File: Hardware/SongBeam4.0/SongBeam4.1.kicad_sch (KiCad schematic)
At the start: 140 parts, among them J1 Conn_01x02, J10 732511150, J11 Conn_01x02, J12 Conn_01x02, J13 Conn_01x01, J2 RJ45, J3 RJ45, J4 Conn_01x07, J5 Conn_01x04, J6 Conn_01x07, J7 Conn_01x04, J8 Conn_01x06, J9 USB_B_Micro, Q2 DTC143ZEBTL, SW2 PTS815 SJM 250 SMTR LFS, SW3 PTS815 SJM 250 SMTR LFS, U1 IM66D132H, U10 Teensy4.1, U11 BQ25185DLHR, U12 AO6604, U13 TPS62842DGRR, U14 TPL5111DDCR, U15 AO6604, U16 TXS0108EPW, U17 LP5907MFX-1.8/NOPB, U19 L86-M33, U2 IM66D132H, U20 AO3407A, U3 IM66D132H, U4 IM66D132H, U5 IM66D132H, U6 IM66D132H, U7 IM66D132H, U8 IM66D132H, U9 PCMD3180IRTWR

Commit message: added a version for manual routing
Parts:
- added F1: Polyfuse, MINISMDC050F-2:MINISMDC050F2, symbol Device:Polyfuse
- R24: value 300 -> 300R
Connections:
- net PWR is gone; now on net +3.3V: J1.1 (Pin_1), JP1.2 (B), U10.48 (VIN)
- net +5V: now also C41.1, R28.1, TP1.1, U12.2 (S2), U13.5 (EN), U13.6 (VIN); no longer F3.1
- net GND: no longer J3.1, J3.2
- net VBAT: now also F1.2; no longer C27.2, U11.2 (BAT)
- net VBUS: now also F3.2; no longer C29.2, U11.10 (IN)
- new net: C29.2, F3.1, U11.10 (IN)
- new net: C27.2, F1.1, U11.2 (BAT)
- no-connect marks 45 -> 47
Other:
- moved on the sheet: C27, C29, F3

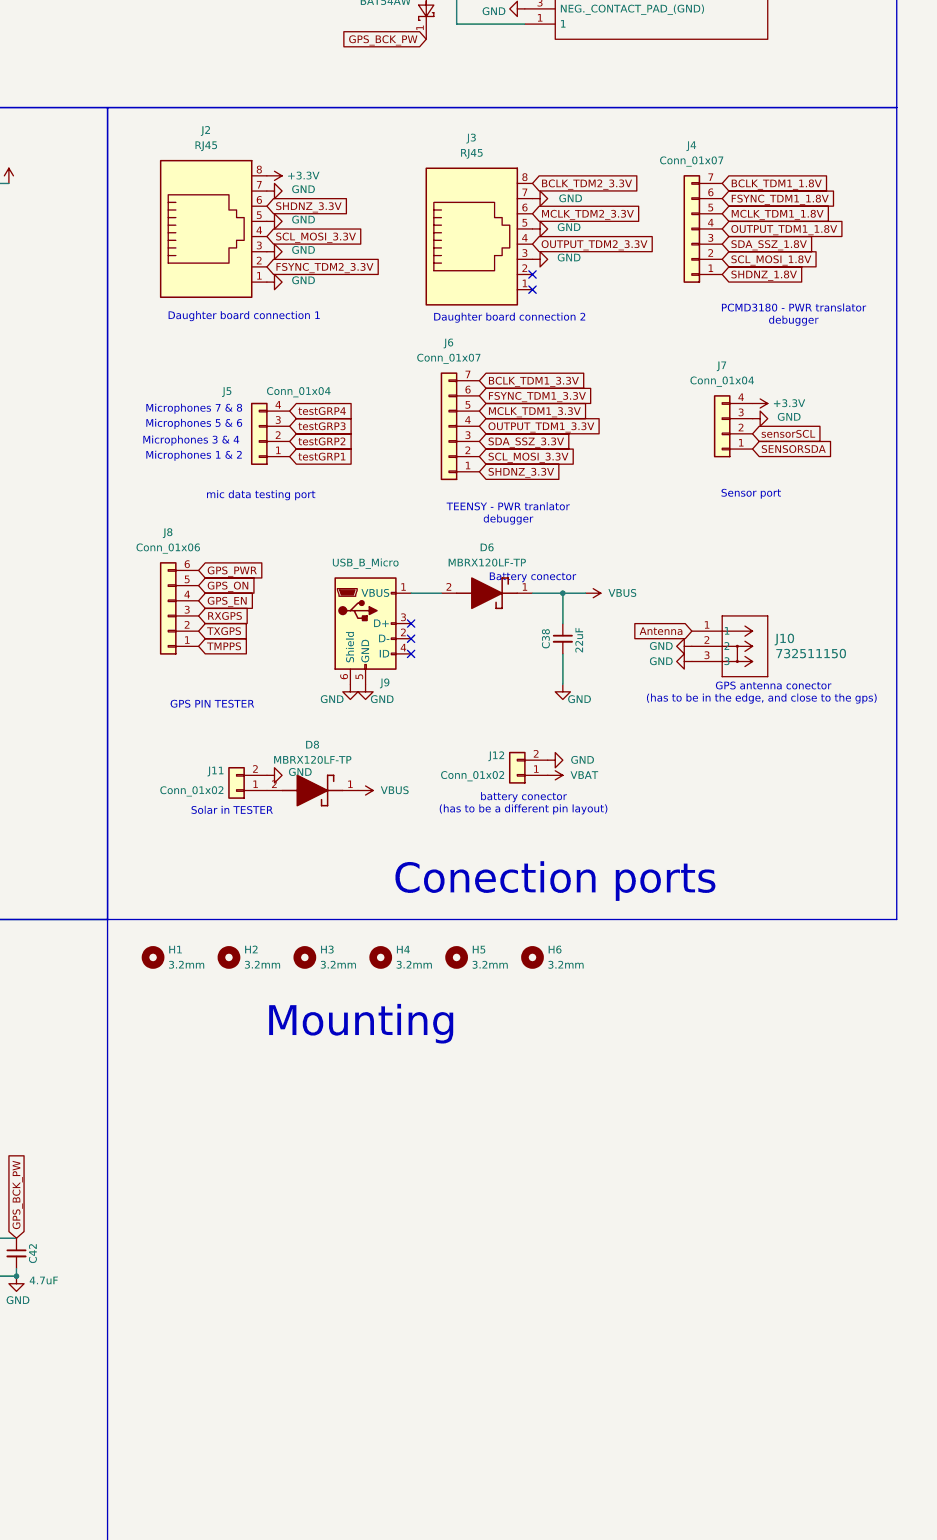
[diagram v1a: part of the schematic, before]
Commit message: ethernet port updated, fixed flaws 1.1 DB
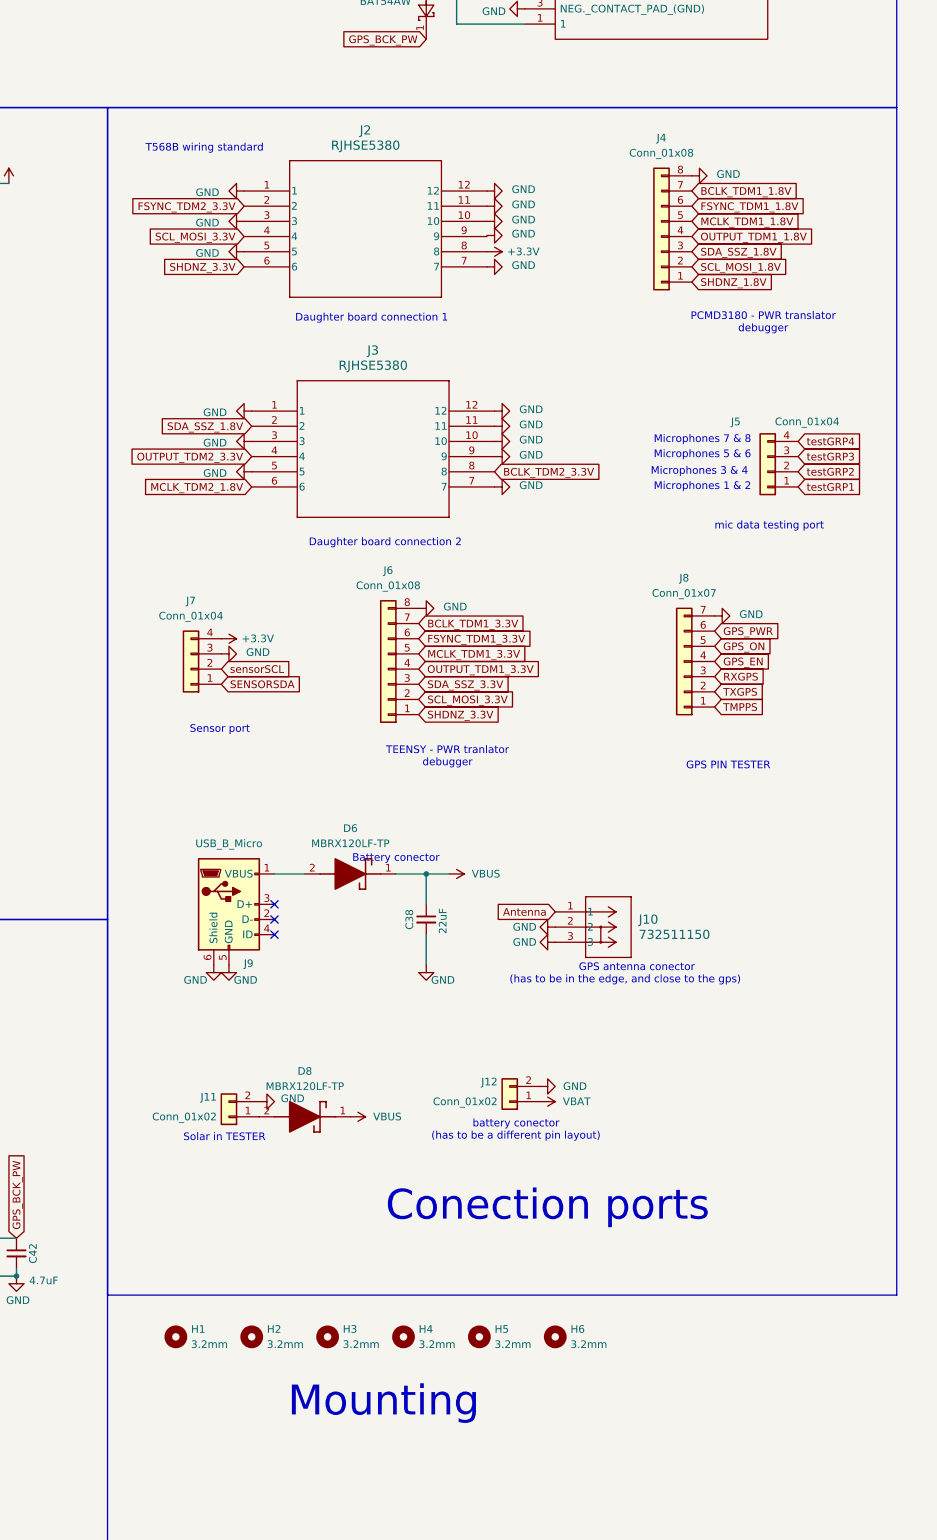
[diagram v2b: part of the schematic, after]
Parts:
- removed J2, J3: RJ45, RJHSE-3380:CONN_RJHSE-3380_AMP, symbol Connector:RJ45
- removed J4, J6: Conn_01x07, Connector_PinHeader_1.00mm:PinHeader_1x07_P1.00mm_Vertical, symbol Connector_Generic:Conn_01x07
- removed J8: Conn_01x06, Connector_PinHeader_1.00mm:PinHeader_1x06_P1.00mm_Vertical, symbol Connector_Generic:Conn_01x06
- added J2, J3: RJHSE5380, RJHSE5380_AMP, symbol Ethernet R/A:RJHSE5380
- added J4, J6: Conn_01x08, symbol Connector_Generic:Conn_01x08
- added J8: Conn_01x07, symbol Connector_Generic:Conn_01x07
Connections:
- net +3.3V: now also J2.8
- net BCLK_TDM1_1.8V: now also J4.7 (Pin_7)
- net BCLK_TDM1_3.3V: now also J6.7 (Pin_7)
- net BCLK_TDM2_3.3V: now also J3.8
- net FSYNC_TDM1_1.8V: now also J4.6 (Pin_6)
- net FSYNC_TDM1_3.3V: now also J6.6 (Pin_6)
- net FSYNC_TDM2_3.3V: now also J2.2
- net GND: now also J2.1, J2.10, J2.11, J2.12, J2.3, J2.5, J2.7, J3.1, J3.10, J3.11, J3.12, J3.3, J3.5, J3.7, J3.9, J4.8 (Pin_8), J6.8 (Pin_8), J8.7 (Pin_7)
- net GPS_EN: now also J8.4 (Pin_4)
- net GPS_ON: now also J8.5 (Pin_5)
- net GPS_PWR: now also J8.6 (Pin_6)
- net MCLK_TDM1_1.8V: now also J4.5 (Pin_5)
- net MCLK_TDM1_3.3V: now also J6.5 (Pin_5)
- net OUTPUT_TDM1_1.8V: now also J4.4 (Pin_4)
- net OUTPUT_TDM1_3.3V: now also J6.4 (Pin_4)
- net OUTPUT_TDM2_3.3V: now also J3.4
- net RXGPS: now also J8.3 (Pin_3)
- net SCL_MOSI_1.8V: now also J4.2 (Pin_2)
- net SCL_MOSI_3.3V: now also J2.4, J6.2 (Pin_2)
- net SDA_SSZ_1.8V: now also J3.2, J4.3 (Pin_3)
- net SDA_SSZ_3.3V: now also J6.3 (Pin_3)
- net SHDNZ_1.8V: now also J4.1 (Pin_1)
- net SHDNZ_3.3V: now also J2.6, J6.1 (Pin_1)
- net TMPPS: now also J8.1 (Pin_1)
- net TXGPS: now also J8.2 (Pin_2)
- new net MCLK_TDM2_1.8V: J3.6
- no-connect marks 47 -> 45
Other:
- note added: "T568B wiring standard"
- moved on the sheet: C38, D6, D8, H1, H2, H3, H4, H5, H6, J10, J11, J12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

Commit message: implemented  ethernet port pcb R/a
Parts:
- J11, J12: footprint Connector_PinHeader_1.00mm:PinHeader_1x02_P1.00mm_Vertical -> Connector_PinHeader_2.00mm:PinHeader_1x02_P2.00mm_Vertical_SMD_Pin1Right
- J13: footprint Connector_PinHeader_1.00mm:PinHeader_1x01_P1.00mm_Vertical -> Connector_PinHeader_2.00mm:PinHeader_1x01_P2.00mm_Vertical
- J2, J3: footprint RJHSE5380_AMP -> RJHSE5380:RJHSE5380_AMP
- J4, J6: footprint (none) -> Connector_PinHeader_2.00mm:PinHeader_1x08_P2.00mm_Vertical
- J8: footprint (none) -> Connector_PinHeader_2.00mm:PinHeader_1x07_P2.00mm_Vertical
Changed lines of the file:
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@@
 			)
 		)
-		(property "Footprint" ""
+		(property "Footprint" "Connector_PinHeader_2.00mm:PinHeader_1x08_P2.00mm_Vertical"
 			(at 496.57 247.65 0)
 			(effects
@@
 			)
 		)
-		(property "Footprint" "Connector_PinHeader_1.00mm:PinHeader_1x01_P1.00mm_Vertical"
+		(property "Footprint" "Connector_PinHeader_2.00mm:PinHeader_1x01_P2.00mm_Vertical"
 			(at 375.92 335.28 0)
 			(effects
@@
 			)
 		)
-		(property "Footprint" "RJHSE5380_AMP"
+		(property "Footprint" "RJHSE5380:RJHSE5380_AMP"
 			(at 473.71 204.47 0)
 			(effects
@@
 			)
 		)
-		(property "Footprint" "Connector_PinHeader_1.00mm:PinHeader_1x02_P1.00mm_Vertical"
+		(property "Footprint" "Connector_PinHeader_2.00mm:PinHeader_1x02_P2.00mm_Vertical_SMD_Pin1Right"
 			(at 516.89 320.04 0)
 			(effects
@@
 			)
 		)
-		(property "Footprint" "Connector_PinHeader_1.00mm:PinHeader_1x02_P1.00mm_Vertical"
+		(property "Footprint" "Connector_PinHeader_2.00mm:PinHeader_1x02_P2.00mm_Vertical_SMD_Pin1Right"
 			(at 469.9 322.58 0)
 			(effects
@@
 			)
 		)
-		(property "Footprint" ""
+		(property "Footprint" "Connector_PinHeader_2.00mm:PinHeader_1x07_P2.00mm_Vertical"
 			(at 546.1 246.38 0)
 			(effects
@@
 			)
 		)
-		(property "Footprint" ""
+		(property "Footprint" "Connector_PinHeader_2.00mm:PinHeader_1x08_P2.00mm_Vertical"
 			(at 542.29 175.26 0)
 			(effects
@@
 			)
 		)
-		(property "Footprint" "RJHSE5380_AMP"
+		(property "Footprint" "RJHSE5380:RJHSE5380_AMP"
 			(at 472.44 167.64 0)
 			(effects
